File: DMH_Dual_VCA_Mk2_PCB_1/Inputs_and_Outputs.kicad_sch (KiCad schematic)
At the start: 20 parts, among them J0 Conn_01x01, J1 TS_Jack_6.35mm_Sw, J2 TS_Jack_6.35mm_Sw, J200 IDC_02x05, J3 TS_Jack_6.35mm_Sw, J4 TS_Jack_6.35mm_Sw, J5 TS_Jack_6.35mm_Sw, J50 Conn_01x08, J6 TS_Jack_6.35mm_Sw, J60 Conn_01x08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

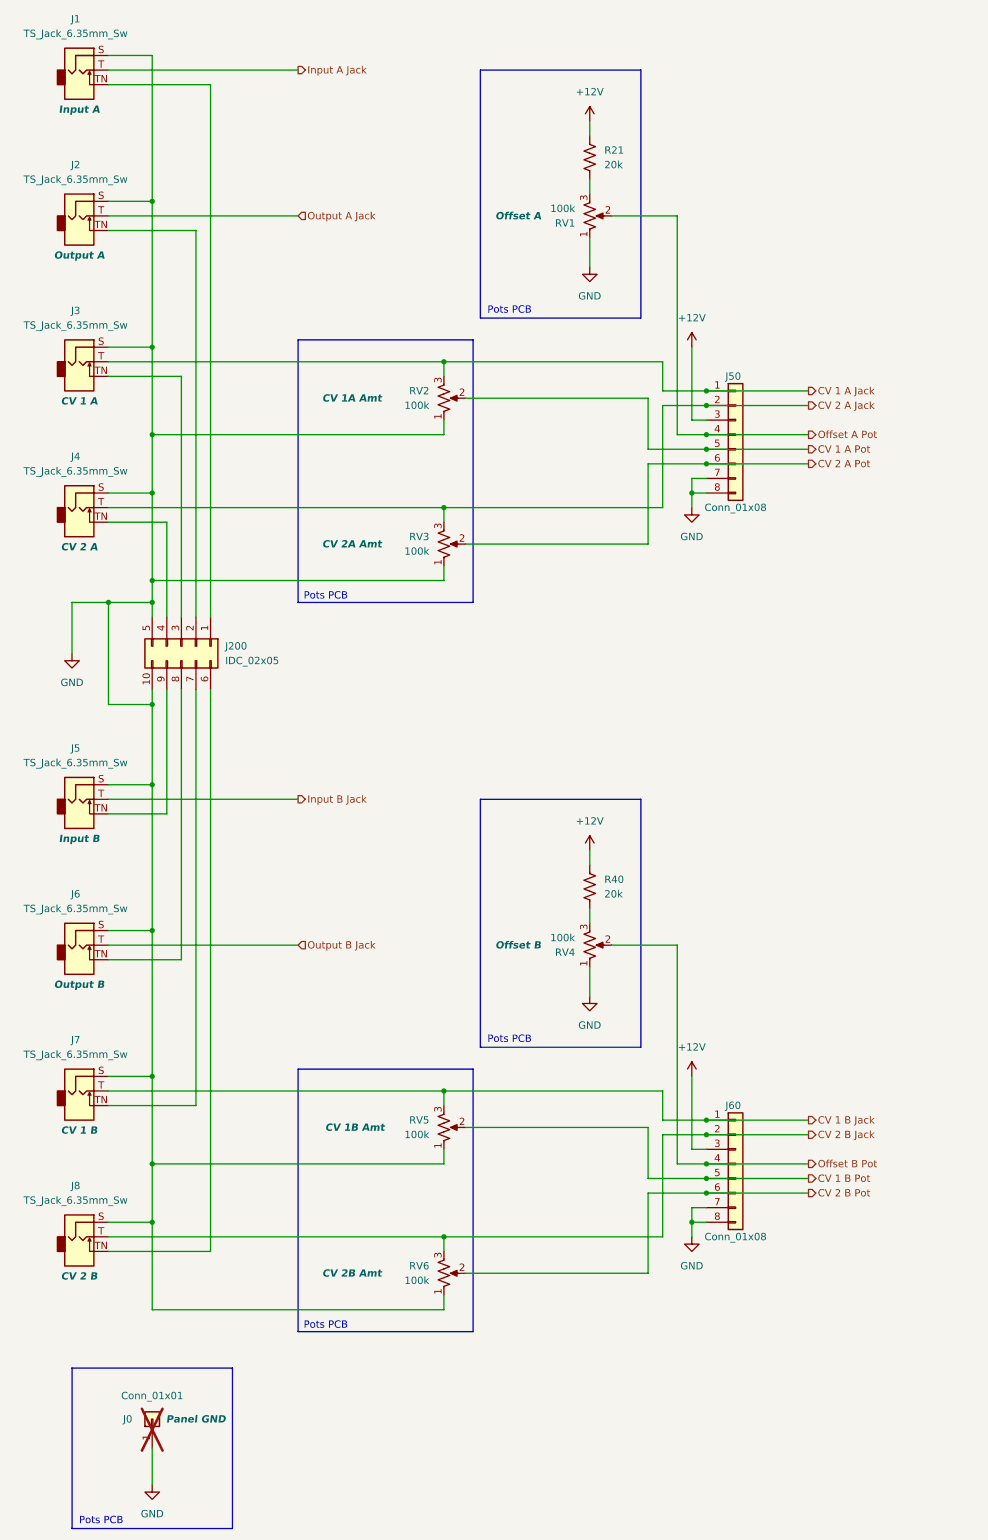
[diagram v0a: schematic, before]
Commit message: Finished schematic for PCB 1
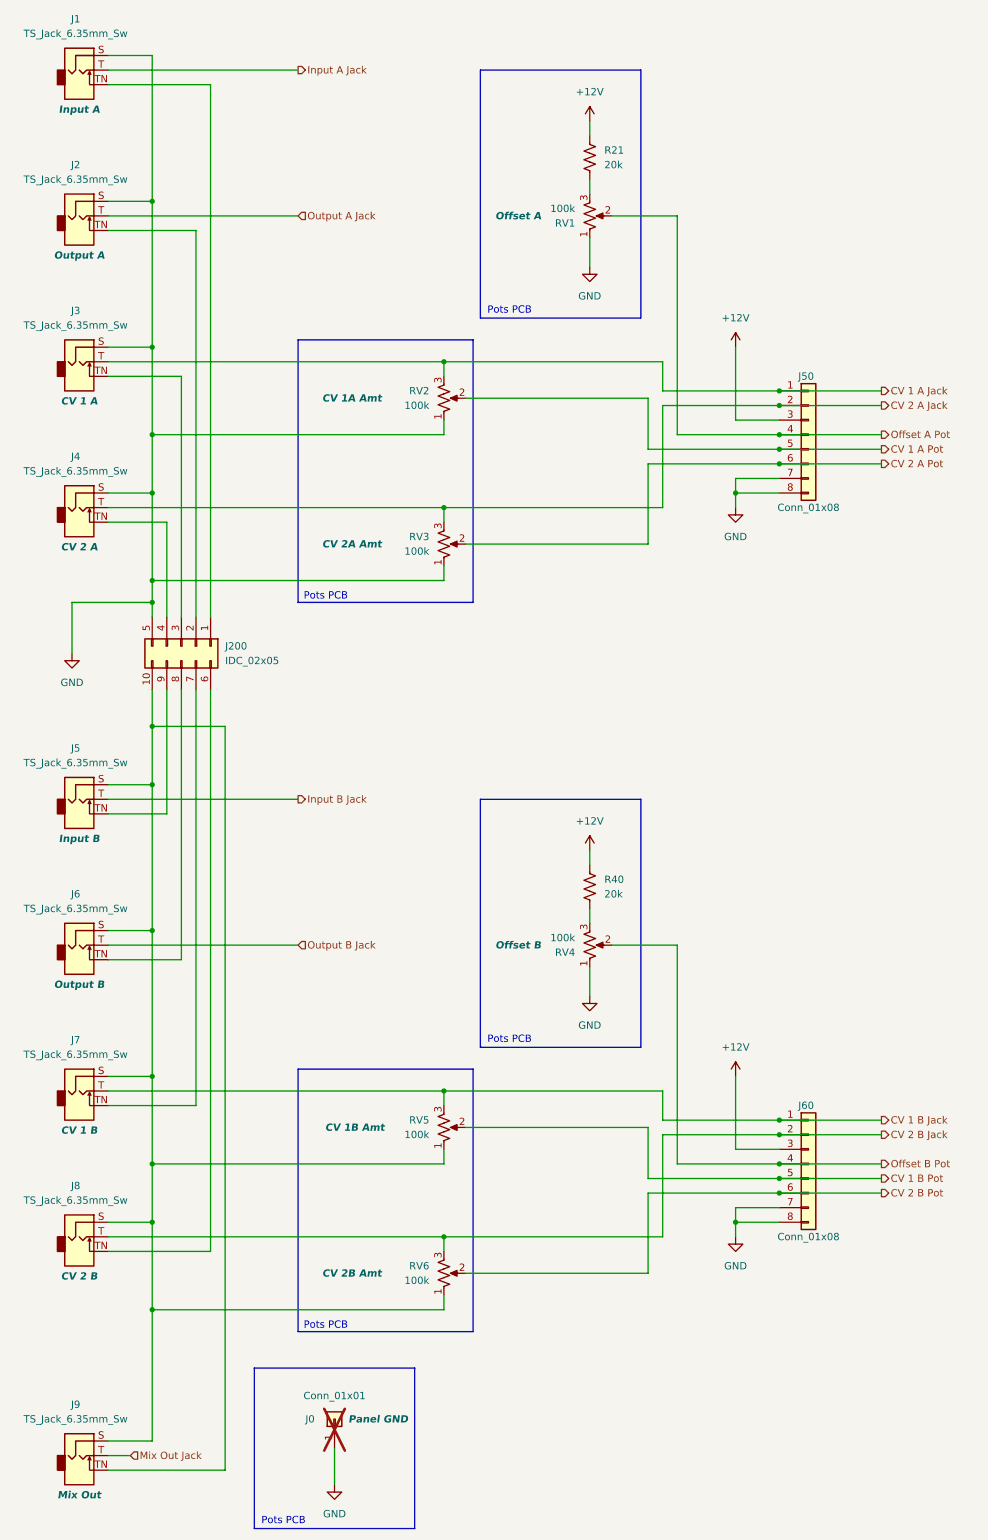
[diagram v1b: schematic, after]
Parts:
- added J9: TS_Jack_6.35mm_Sw, SynthStuff:CUI_MJ-63052A, symbol SynthStuff:TS_Jack_6.35mm_Sw
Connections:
- net GND: no longer J200.10 (Pin_10), J5.S, J6.S, J7.S, J8.S, RV5.1, RV6.1
- new net: J200.10 (Pin_10), J5.S, J6.S, J7.S, J8.S, J9.S, J9.TN, RV5.1, RV6.1
- new net Mix Out Jack: J9.T
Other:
- moved on the sheet: J0, J50, J60

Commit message: Added missing GND to lower jacks
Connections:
- net GND: now also J200.10 (Pin_10), J5.S, J6.S, J7.S, J8.S, J9.S, J9.TN, RV5.1, RV6.1
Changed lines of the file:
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@@
+	)
+	(junction
+		(at 30.48 118.11)
+		(diameter 0)
+		(color 0 0 0 0)
 	)
 	(junction
@@
 	(wire
 		(pts
-			(xy 24.13 118.11) (xy 38.1 118.11)
+			(xy 24.13 118.11) (xy 30.48 118.11)
 		)
 		(stroke
@@
 	(wire
 		(pts
+			(xy 30.48 118.11) (xy 38.1 118.11)
+		)
+		(stroke
+			(width 0)
+			(type default)
+		)
+	)
+	(wire
+		(pts
 			(xy 38.1 48.26) (xy 38.1 73.66)
 		)
@@
 	(wire
 		(pts
+			(xy 38.1 139.7) (xy 30.48 139.7)
+		)
+		(stroke
+			(width 0)
+			(type default)
+		)
+	)
+	(wire
+		(pts
 			(xy 30.48 175.26) (xy 38.1 175.26)
 		)
@@
 		)
 		(stroke
+			(width 0)
+			(type default)
+		)
+	)
+	(wire
+		(pts
+			(xy 30.48 139.7) (xy 30.48 118.11)
+		)
+		(stroke
